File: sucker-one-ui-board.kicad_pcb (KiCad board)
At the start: 4 copper layers, 36.4 x 48.3 mm, 49 parts, among them J1 BM10B-SRSS-TB(LF)(SN), SW1 LIFT, SW2 LOW, SW3 REVERSE, SW4 TRIGGER, SW5 DROP, SW6 HIGH, U1 WS2812-2020, U10 WS2812-2020, U11 WS2812-2020, U12 WS2812-2020, U2 WS2812-2020, U3 WS2812-2020, U4 WS2812-2020, U5 WS2812-2020, U6 WS2812-2020, U7 WS2812-2020, U8 WS2812-2020, U9 WS2812-2020

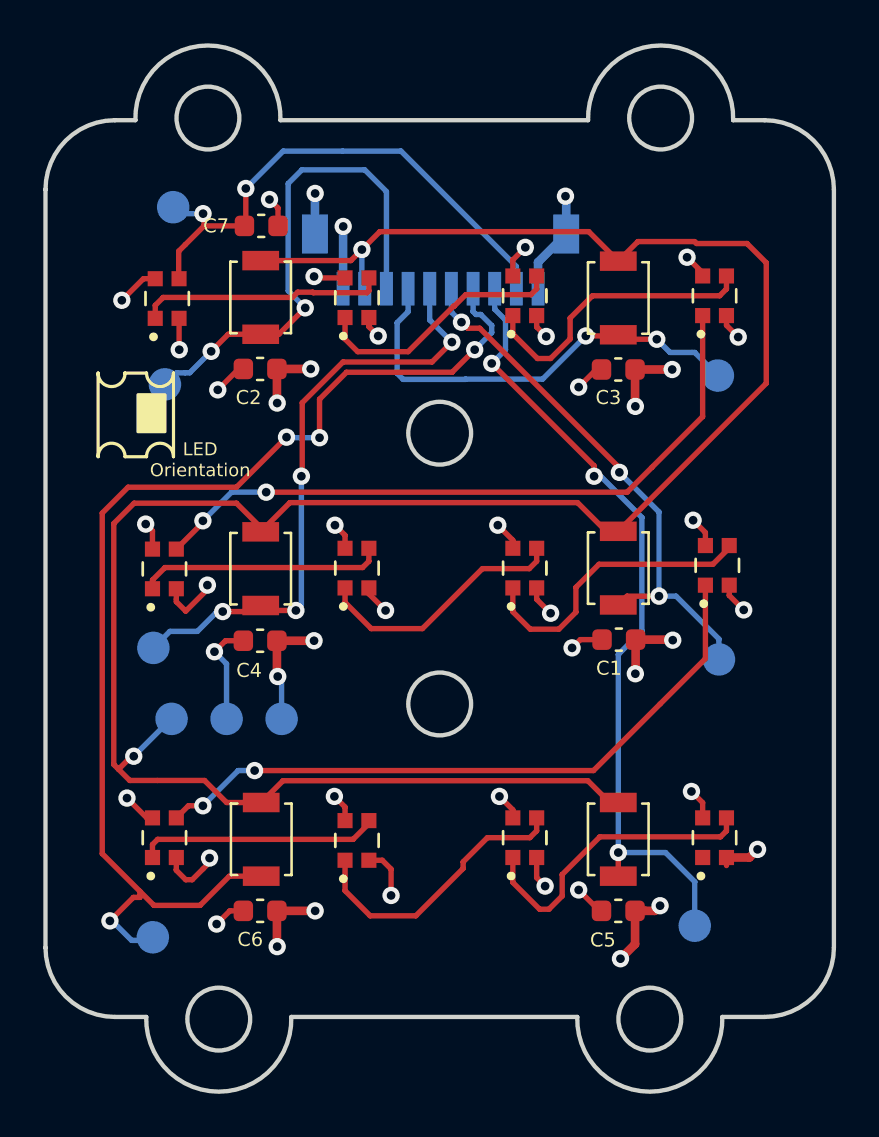
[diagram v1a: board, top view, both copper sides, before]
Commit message: Update project to Kicad 6
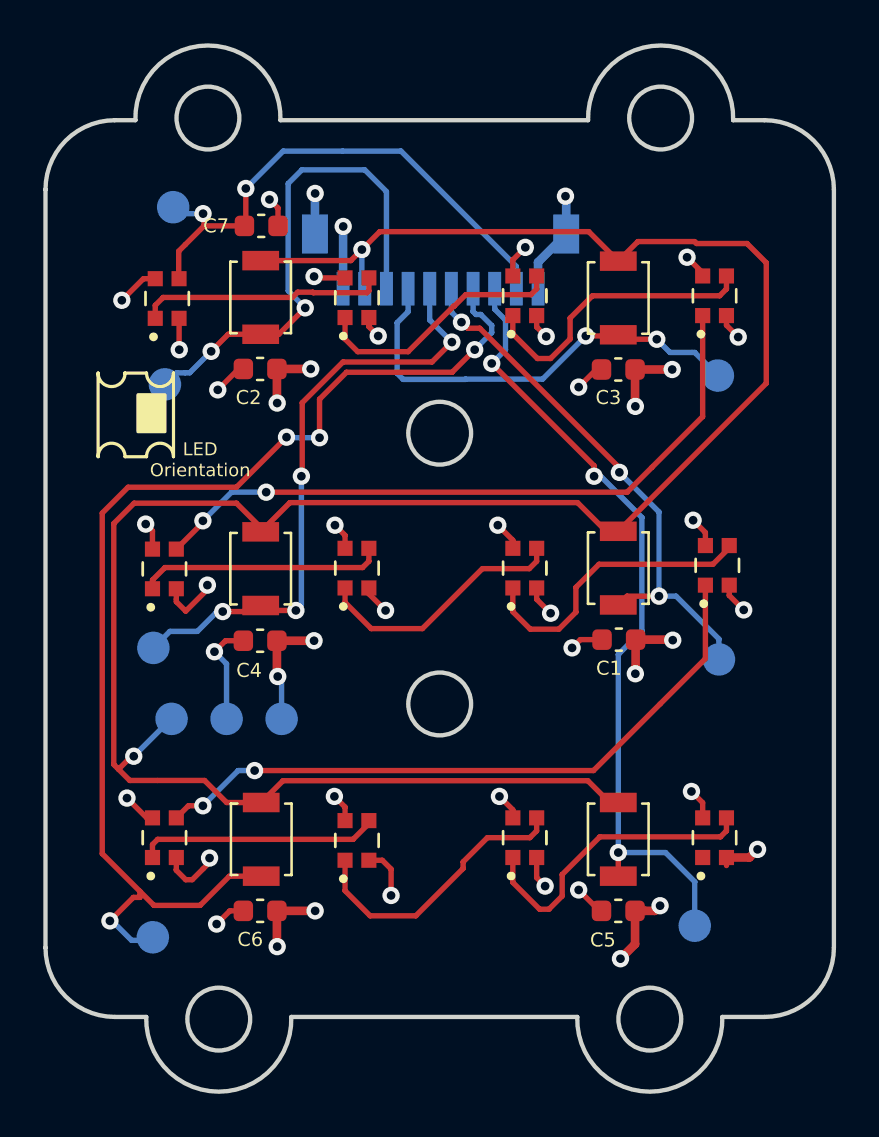
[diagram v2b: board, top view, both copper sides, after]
